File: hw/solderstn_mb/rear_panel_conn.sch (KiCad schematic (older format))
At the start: 17 parts, among them J1201 USB_A-TE_1-292303-1, J1202 DB9_Male_MountingHoles, J1203 USB_B-TE_1734346-1, U1201 USBLC6-2SC6, U1202 USBLC6-2SC6

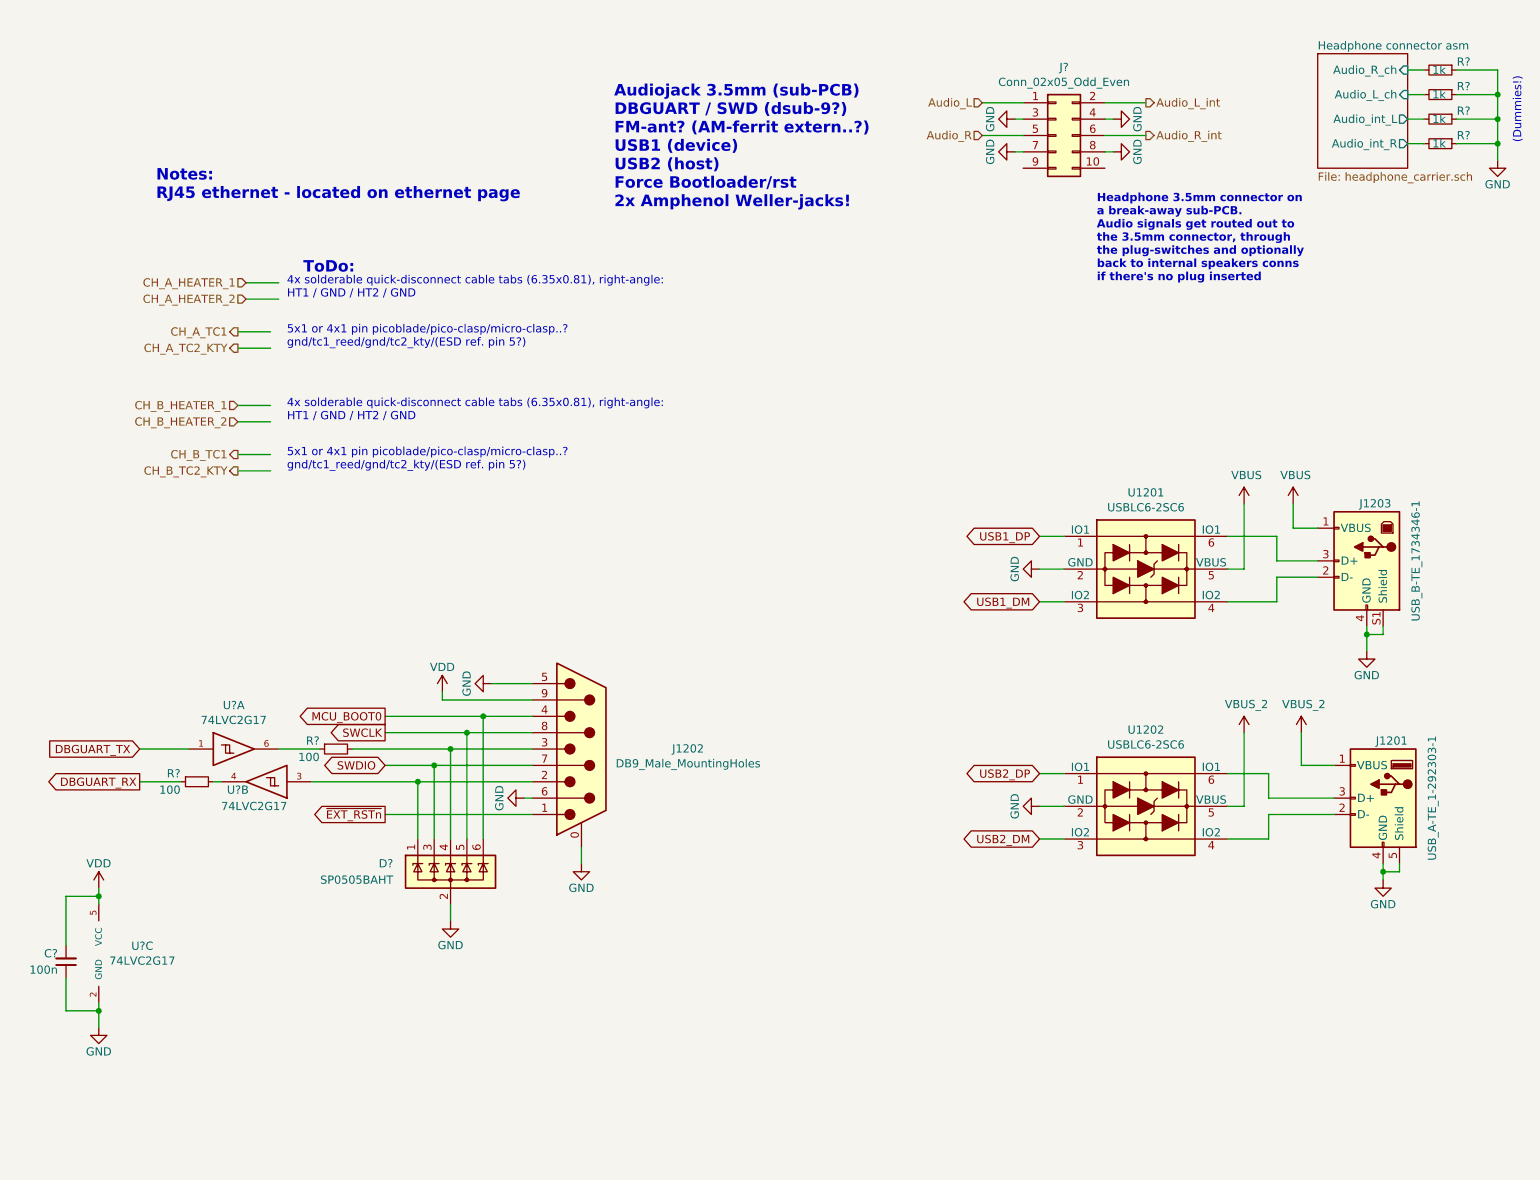
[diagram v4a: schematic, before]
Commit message: Updated display-board sch & PCB with optional left-hand rotary encoder instead of pwrbtn. Printed MB schematic updates PDF for 20-08-21
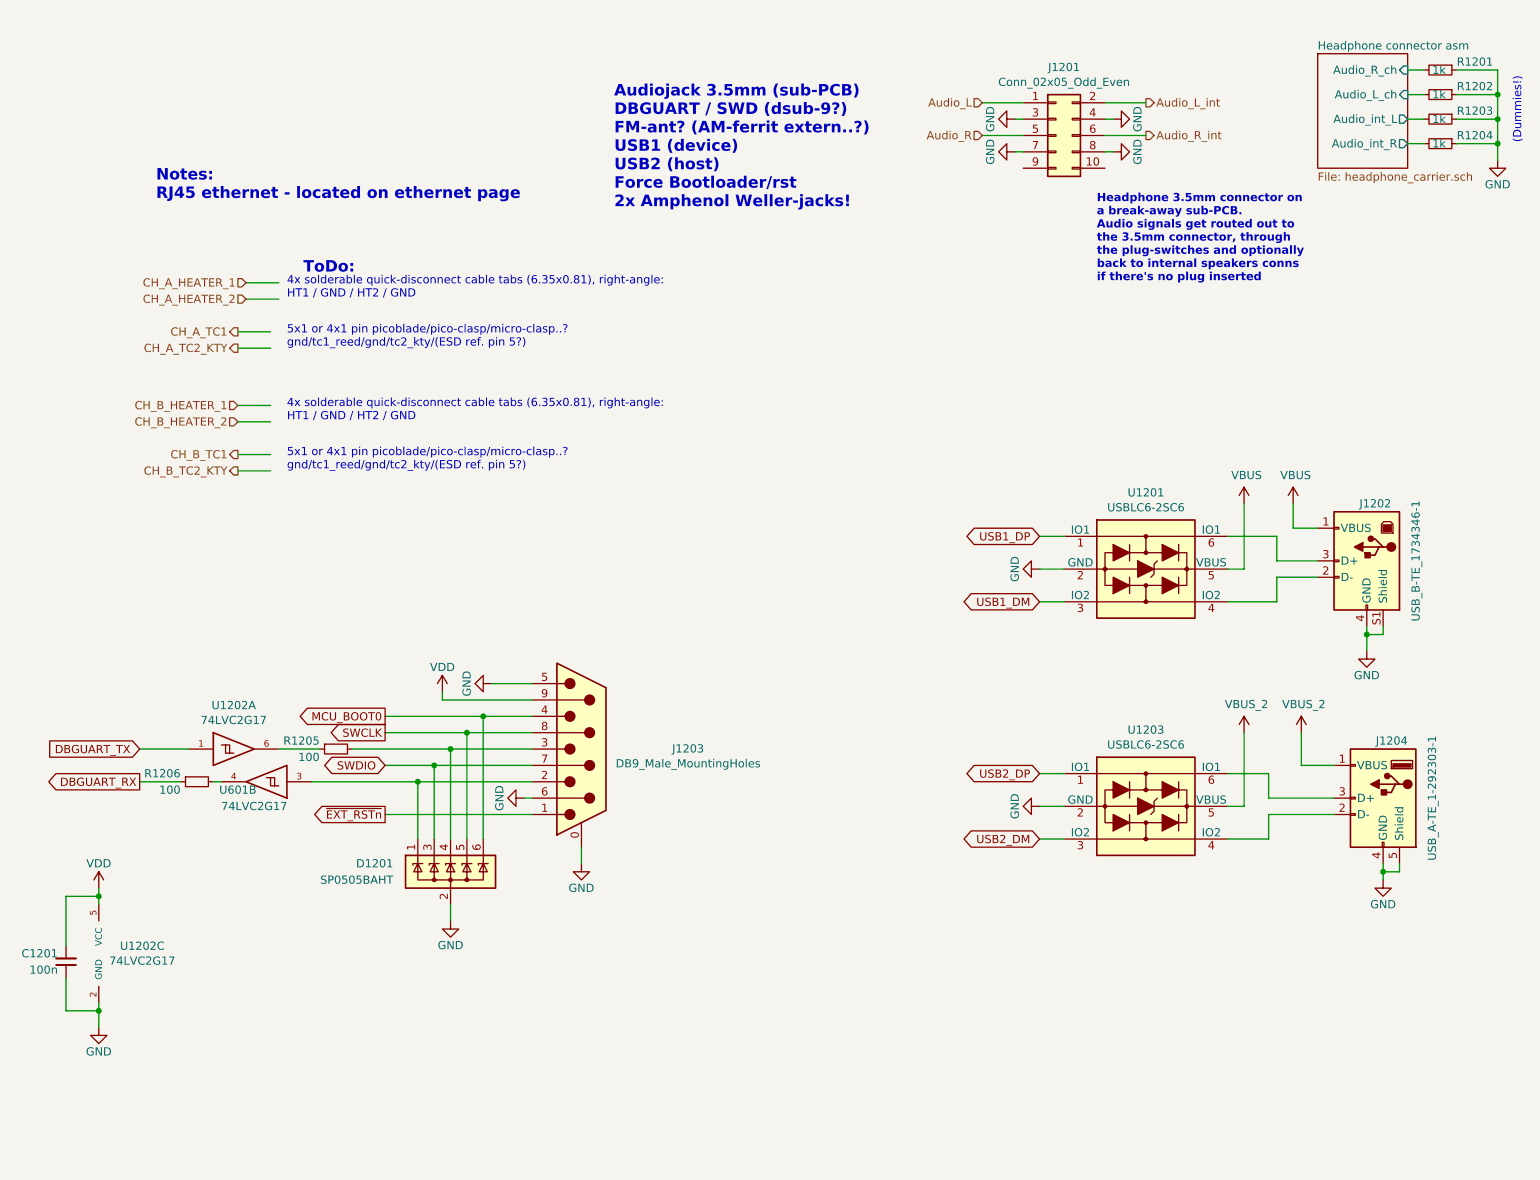
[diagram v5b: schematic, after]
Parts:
- gave numbers to parts that had none: 11
- renumbered J1203 to J1202, J1202 to J1203, J1201 to J1204, U1202 to U1203
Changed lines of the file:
@@
 Notes:\nRJ45 ethernet - located on ethernet page\n
 $Comp
-L customlib_mj:USB_A-TE_1-292303-1 J1201
+L customlib_mj:USB_A-TE_1-292303-1 J1204
 U 1 1 5F769C5C
 P 9250 5500
-F 0 "J1201" H 9100 5850 50  0000 L CNN
+F 0 "J1204" H 9100 5850 50  0000 L CNN
 F 1 "USB_A-TE_1-292303-1" V 8950 5500 50  0000 C CNN
 F 2 "customlib_mj_fp:TE_1-292303-1" H 9400 5450 50  0001 C CNN
@@
 $EndComp
 $Comp
-L customlib_mj:USB_B-TE_1734346-1 J1203
+L customlib_mj:USB_B-TE_1734346-1 J1202
 U 1 1 5F76B363
 P 9150 4050
-F 0 "J1203" H 9000 4400 50  0000 L CNN
+F 0 "J1202" H 9000 4400 50  0000 L CNN
 F 1 "USB_B-TE_1734346-1" V 8850 4050 50  0000 C CNN
 F 2 "customlib_mj_fp:TE_1734346" H 9300 4000 50  0001 C CNN
@@
 	8550 5600 8950 5600
 $Comp
-L power:GND #PWR01207
+L power:GND #PWR01209
 U 1 1 5F76C43A
 P 9150 4600
-F 0 "#PWR01207" H 9150 4350 50  0001 C CNN
+F 0 "#PWR01209" H 9150 4350 50  0001 C CNN
 F 1 "GND" H 9150 4450 50  0000 C CNN
 F 2 "" H 9150 4600 50  0001 C CNN
@@
 $EndComp
 $Comp
-L power:GND #PWR01204
+L power:GND #PWR01217
 U 1 1 5F76C9A9
 P 9250 6000
-F 0 "#PWR01204" H 9250 5750 50  0001 C CNN
+F 0 "#PWR01217" H 9250 5750 50  0001 C CNN
 F 1 "GND" H 9250 5850 50  0000 C CNN
 F 2 "" H 9250 6000 50  0001 C CNN
@@
 	9150 4500 9150 4600
 $Comp
-L customlib_mj:VBUS_2 #PWR01201
+L customlib_mj:VBUS_2 #PWR01213
 U 1 1 5F77B5A7
 P 8750 5100
-F 0 "#PWR01201" H 8750 4950 50  0001 C CNN
+F 0 "#PWR01213" H 8750 4950 50  0001 C CNN
 F 1 "VBUS_2" H 8765 5273 50  0000 C CNN
 F 2 "" H 8750 5100 50  0001 C CNN
@@
 	8750 5300 8750 5100
 $Comp
-L customlib_mj:VBUS #PWR01206
+L customlib_mj:VBUS #PWR01207
 U 1 1 5F77C454
 P 8700 3700
-F 0 "#PWR01206" H 8700 3550 50  0001 C CNN
+F 0 "#PWR01207" H 8700 3550 50  0001 C CNN
 F 1 "VBUS" H 8715 3873 50  0000 C CNN
 F 2 "" H 8700 3700 50  0001 C CNN
@@
 	8600 4150 8850 4150
 $Comp
-L Connector:DB9_Male_MountingHoles J1202
+L Connector:DB9_Male_MountingHoles J1203
 U 1 1 5F3A1DC2
 P 4350 5200
-F 0 "J1202" H 5002 5202 50  0000 C CNN
+F 0 "J1203" H 5002 5202 50  0000 C CNN
 F 1 "DB9_Male_MountingHoles" H 5002 5111 50  0000 C CNN
 F 2 "Connector_Dsub:DSUB-9_Male_Horizontal_P2.77x2.84mm_EdgePinOffset9.90mm_Housed_MountingHolesOffset11.32mm" H 4350 5200 50  0001 C CNN
@@
 $EndComp
 $Comp
-L power:GND #PWR01202
+L power:GND #PWR01210
 U 1 1 5F3B8CBB
 P 3800 4800
-F 0 "#PWR01202" H 3800 4550 50  0001 C CNN
+F 0 "#PWR01210" H 3800 4550 50  0001 C CNN
 F 1 "GND" H 3800 4650 50  0000 C CNN
 F 2 "" H 3800 4800 50  0001 C CNN
@@
 SWDIO
 $Comp
-L power:VDD #PWR01203
+L power:VDD #PWR01211
 U 1 1 5F3B9A5E
 P 3500 4850
-F 0 "#PWR01203" H 3500 4700 50  0001 C CNN
+F 0 "#PWR01211" H 3500 4700 50  0001 C CNN
 F 1 "VDD" H 3500 5000 50  0000 C CNN
 F 2 "" H 3500 4850 50  0001 C CNN
@@
 	3500 4900 4050 4900
 $Comp
-L power:GND #PWR01205
+L power:GND #PWR01214
 U 1 1 5F3BB41A
 P 4000 5500
-F 0 "#PWR01205" H 4000 5250 50  0001 C CNN
+F 0 "#PWR01214" H 4000 5250 50  0001 C CNN
 F 1 "GND" H 4000 5350 50  0000 C CNN
 F 2 "" H 4000 5500 50  0001 C CNN
@@
 	4050 5500 4000 5500
 $Comp
-L customlib_mj:USBLC6-2SC6 U1202
+L customlib_mj:USBLC6-2SC6 U1203
 U 1 1 5F3C08E8
 P 7800 5550
-F 0 "U1202" H 7800 6017 50  0000 C CNN
+F 0 "U1203" H 7800 6017 50  0000 C CNN
 F 1 "USBLC6-2SC6" H 7800 5926 50  0000 C CNN
 F 2 "TO_SOT_Packages_SMD:SOT-23-6" H 8450 5900 50  0001 C CNN
@@
 	7050 1450 6800 1450
 $Comp
-L power:GND #PWR?
+L power:GND #PWR01201
 U 1 1 5F924C25
 P 7000 1350
-F 0 "#PWR?" H 7000 1100 50  0001 C CNN
+F 0 "#PWR01201" H 7000 1100 50  0001 C CNN
 F 1 "GND" H 7000 1200 50  0000 C CNN
 F 2 "" H 7000 1350 50  0001 C CNN
@@
 $EndComp
 $Comp
-L power:GND #PWR?
+L power:GND #PWR01202
 U 1 1 5F925961
 P 7600 1350
-F 0 "#PWR?" H 7600 1100 50  0001 C CNN
+F 0 "#PWR01202" H 7600 1100 50  0001 C CNN
 F 1 "GND" H 7600 1200 50  0000 C CNN
 F 2 "" H 7600 1350 50  0001 C CNN
@@
 	7050 1350 7000 1350
 $Comp
-L Device:R_Small R?
+L Device:R_Small R1201
 U 1 1 5F929D46
 P 9600 1050
-F 0 "R?" V 9550 1150 50  0000 L CNN
+F 0 "R1201" V 9550 1150 50  0000 L CNN
 F 1 "1k" V 9600 1000 50  0000 L CNN
 F 2 "" H 9600 1050 50  0001 C CNN
@@
 $EndComp
 $Comp
-L Device:R_Small R?
+L Device:R_Small R1202
 U 1 1 5F92A4C3
 P 9600 1200
-F 0 "R?" V 9550 1300 50  0000 L CNN
+F 0 "R1202" V 9550 1300 50  0000 L CNN
 F 1 "1k" V 9600 1150 50  0000 L CNN
 F 2 "" H 9600 1200 50  0001 C CNN
@@
 $EndComp
 $Comp
-L Device:R_Small R?
+L Device:R_Small R1203
 U 1 1 5F92A665
 P 9600 1350
-F 0 "R?" V 9550 1450 50  0000 L CNN
+F 0 "R1203" V 9550 1450 50  0000 L CNN
 F 1 "1k" V 9600 1300 50  0000 L CNN
 F 2 "" H 9600 1350 50  0001 C CNN
@@
 $EndComp
 $Comp
-L Device:R_Small R?
+L Device:R_Small R1204
 U 1 1 5F92A880
 P 9600 1500
-F 0 "R?" V 9550 1600 50  0000 L CNN
+F 0 "R1204" V 9550 1600 50  0000 L CNN
 F 1 "1k" V 9600 1450 50  0000 L CNN
 F 2 "" H 9600 1500 50  0001 C CNN
@@
 $EndComp
 $Comp
-L power:GND #PWR?
+L power:GND #PWR01205
 U 1 1 5F92BA81
 P 9950 1600
-F 0 "#PWR?" H 9950 1350 50  0001 C CNN
+F 0 "#PWR01205" H 9950 1350 50  0001 C CNN
 F 1 "GND" H 9950 1450 50  0000 C CNN
 F 2 "" H 9950 1600 50  0001 C CNN
@@
 	8550 5750 8300 5750
 $Comp
-L power:GND #PWR?
+L power:GND #PWR01215
 U 1 1 5F992016
 P 7150 5550
-F 0 "#PWR?" H 7150 5300 50  0001 C CNN
+F 0 "#PWR01215" H 7150 5300 50  0001 C CNN
 F 1 "GND" H 7150 5400 50  0000 C CNN
 F 2 "" H 7150 5550 50  0001 C CNN
@@
 	8400 5550 8400 5100
 $Comp
-L customlib_mj:VBUS_2 #PWR?
+L customlib_mj:VBUS_2 #PWR01212
 U 1 1 5F995BB7
 P 8400 5100
-F 0 "#PWR?" H 8400 4950 50  0001 C CNN
+F 0 "#PWR01212" H 8400 4950 50  0001 C CNN
 F 1 "VBUS_2" H 8415 5273 50  0000 C CNN
 F 2 "" H 8400 5100 50  0001 C CNN
@@
 	8400 4100 8400 3700
 $Comp
-L customlib_mj:VBUS #PWR?
+L customlib_mj:VBUS #PWR01206
 U 1 1 5F99E9EF
 P 8400 3700
-F 0 "#PWR?" H 8400 3550 50  0001 C CNN
+F 0 "#PWR01206" H 8400 3550 50  0001 C CNN
 F 1 "VBUS" H 8415 3873 50  0000 C CNN
 F 2 "" H 8400 3700 50  0001 C CNN
@@
 $EndComp
 $Comp
-L power:GND #PWR?
+L power:GND #PWR01208
 U 1 1 5F99EC1F
 P 7150 4100
-F 0 "#PWR?" H 7150 3850 50  0001 C CNN
+F 0 "#PWR01208" H 7150 3850 50  0001 C CNN
 F 1 "GND" H 7150 3950 50  0000 C CNN
 F 2 "" H 7150 4100 50  0001 C CNN
@@
 	7150 4300 7300 4300
 $Comp
-L customlib_mj:74LVC2G17 U?
+L customlib_mj:74LVC2G17 U1202
 U 1 1 5F9A79CF
 P 2250 5200
-F 0 "U?" H 2225 5467 50  0000 C CNN
+F 0 "U1202" H 2225 5467 50  0000 C CNN
 F 1 "74LVC2G17" H 2225 5376 50  0000 C CNN
 F 2 "" H 2250 5200 50  0001 C CNN
@@
 $EndComp
 $Comp
-L customlib_mj:74LVC2G17 U?
+L customlib_mj:74LVC2G17 U601
 U 2 1 5F9A89B3
 P 2400 5400
-F 0 "U?" H 2550 5450 50  0000 C CNN
+F 0 "U601" H 2550 5450 50  0000 C CNN
 F 1 "74LVC2G17" H 2450 5550 50  0000 C CNN
 F 2 "" H 2400 5400 50  0001 C CNN
@@
 $EndComp
 $Comp
-L customlib_mj:74LVC2G17 U?
+L customlib_mj:74LVC2G17 U1202
 U 3 1 5F9A92DC
 P 1400 6450
-F 0 "U?" H 1666 6496 50  0000 C CNN
+F 0 "U1202" H 1666 6496 50  0000 C CNN
 F 1 "74LVC2G17" H 1666 6405 50  0000 C CNN
 F 2 "" H 1400 6450 50  0001 C CNN
@@
 $EndComp
 $Comp
-L Device:R_Small R?
+L Device:R_Small R1205
 U 1 1 5F9AE0AD
 P 2850 5200
-F 0 "R?" V 2800 5300 50  0000 L CNN
+F 0 "R1205" V 2800 5300 50  0000 L CNN
 F 1 "100" V 2900 5300 50  0000 L CNN
 F 2 "" H 2850 5200 50  0001 C CNN
@@
 	1950 5200 1650 5200
 $Comp
-L Device:R_Small R?
+L Device:R_Small R1206
 U 1 1 5F9B98A1
 P 2000 5400
-F 0 "R?" V 1950 5500 50  0000 L CNN
+F 0 "R1206" V 1950 5500 50  0000 L CNN
 F 1 "100" V 2050 5500 50  0000 L CNN
 F 2 "" H 2000 5400 50  0001 C CNN
@@
 	1900 5400 1650 5400
 $Comp
-L power:VDD #PWR?
+L power:VDD #PWR01218
 U 1 1 5F9C015F
 P 1400 6050
-F 0 "#PWR?" H 1400 5900 50  0001 C CNN
+F 0 "#PWR01218" H 1400 5900 50  0001 C CNN
 F 1 "VDD" H 1400 6200 50  0000 C CNN
 F 2 "" H 1400 6050 50  0001 C CNN
@@
 $EndComp
 $Comp
-L power:GND #PWR?
+L power:GND #PWR01220
 U 1 1 5F9C062D
 P 1400 6900
-F 0 "#PWR?" H 1400 6650 50  0001 C CNN
+F 0 "#PWR01220" H 1400 6650 50  0001 C CNN
 F 1 "GND" H 1400 6750 50  0000 C CNN
 F 2 "" H 1400 6900 50  0001 C CNN
@@
 	1400 6150 1400 6100
 $Comp
-L Device:C_Small C?
+L Device:C_Small C1201
 U 1 1 5F9C93AD
 P 1200 6500
-F 0 "C?" H 1250 6450 50  0000 L CNN
+F 0 "C1201" H 1250 6450 50  0000 L CNN
 F 1 "100n" H 1250 6550 50  0000 L CNN
 F 2 "" H 1200 6500 50  0001 C CNN
@@
 	1400 6100 1400 6050
 $Comp
-L power:GND #PWR?
+L power:GND #PWR01216
 U 1 1 5F9D5D95
 P 4350 5900
-F 0 "#PWR?" H 4350 5650 50  0001 C CNN
+F 0 "#PWR01216" H 4350 5650 50  0001 C CNN
 F 1 "GND" H 4350 5750 50  0000 C CNN
 F 2 "" H 4350 5900 50  0001 C CNN
@@
 	4350 5900 4350 5800
 $Comp
-L Power_Protection:SP0505BAHT D?
+L Power_Protection:SP0505BAHT D1201
 U 1 1 5F9D8F09
 P 3550 5950
-F 0 "D?" H 3200 6000 50  0000 R CNN
+F 0 "D1201" H 3200 6000 50  0000 R CNN
 F 1 "SP0505BAHT" H 3200 5900 50  0000 R CNN
 F 2 "Package_TO_SOT_SMD:SOT-23-6" H 3850 5900 50  0001 L CNN
@@
 $EndComp
 $Comp
-L power:GND #PWR?
+L power:GND #PWR01219
 U 1 1 5F9F5C0C
 P 3550 6250
-F 0 "#PWR?" H 3550 6000 50  0001 C CNN
+F 0 "#PWR01219" H 3550 6000 50  0001 C CNN
 F 1 "GND" H 3550 6100 50  0000 C CNN
 F 2 "" H 3550 6250 50  0001 C CNN
@@
 	3750 5000 4050 5000
 $Comp
-L Connector_Generic:Conn_02x05_Odd_Even J?
+L Connector_Generic:Conn_02x05_Odd_Even J1201
 U 1 1 5FA2CF9B
 P 7250 1450
-F 0 "J?" H 7300 1867 50  0000 C CNN
+F 0 "J1201" H 7300 1867 50  0000 C CNN
 F 1 "Conn_02x05_Odd_Even" H 7300 1776 50  0000 C CNN
 F 2 "Connector_PinSocket_2.54mm:PinSocket_2x05_P2.54mm_Vertical" H 7250 1450 50  0001 C CNN
@@
 $EndComp
 $Comp
-L power:GND #PWR?
+L power:GND #PWR01203
 U 1 1 5FA2DA97
 P 7000 1550
-F 0 "#PWR?" H 7000 1300 50  0001 C CNN
+F 0 "#PWR01203" H 7000 1300 50  0001 C CNN
 F 1 "GND" H 7000 1400 50  0000 C CNN
 F 2 "" H 7000 1550 50  0001 C CNN
@@
 $EndComp
 $Comp
-L power:GND #PWR?
+L power:GND #PWR01204
 U 1 1 5FA2DDB5
 P 7600 1550
-F 0 "#PWR?" H 7600 1300 50  0001 C CNN
+F 0 "#PWR01204" H 7600 1300 50  0001 C CNN
 F 1 "GND" H 7600 1400 50  0000 C CNN
 F 2 "" H 7600 1550 50  0001 C CNN
